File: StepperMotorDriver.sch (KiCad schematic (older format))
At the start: 15 parts, among them J2 Conn_01x04_Male, U1 DRV8825PWPR

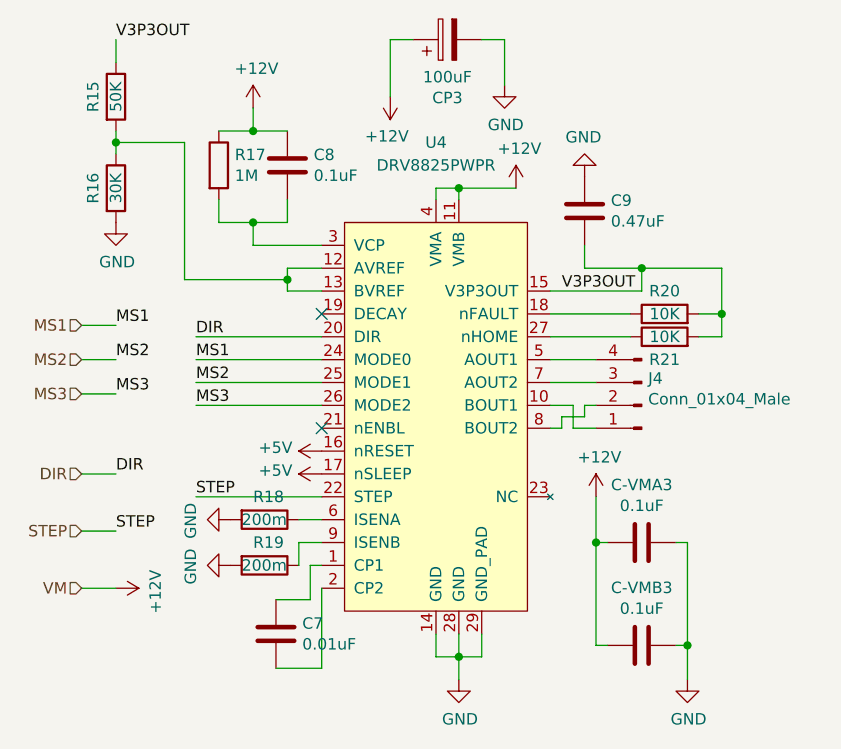
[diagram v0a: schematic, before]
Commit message: Test Pin
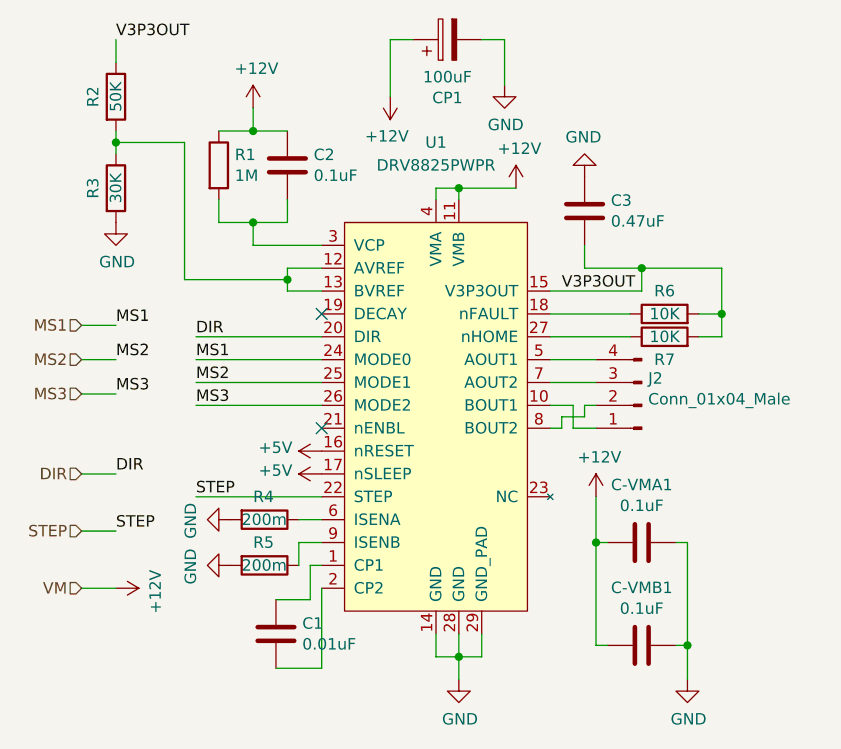
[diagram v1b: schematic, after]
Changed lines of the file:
@@
 $Descr A4 11693 8268
 encoding utf-8
-Sheet 3 10
+Sheet 4 10
 Title ""
 Date ""
@@
 AR Path="/5E601D92/5E5CA1CC" Ref="#PWR0118"  Part="1"
 AR Path="/5E6050A3/5E5CA1CC" Ref="#PWR0133"  Part="1"
-F 0 "#PWR0133" H 5950 4050 50  0001 C CNN
+F 0 "#PWR0101" H 5950 4050 50  0001 C CNN
 F 1 "GND" H 5955 4127 50  0000 C CNN
 F 2 "" H 5950 4300 50  0001 C CNN
@@
 AR Path="/5E601D92/5E5CAE8A" Ref="#PWR0119"  Part="1"
 AR Path="/5E6050A3/5E5CAE8A" Ref="#PWR0134"  Part="1"
-F 0 "#PWR0134" H 4450 2050 50  0001 C CNN
+F 0 "#PWR0102" H 4450 2050 50  0001 C CNN
 F 1 "GND" H 4455 2127 50  0000 C CNN
 F 2 "" H 4450 2300 50  0001 C CNN
@@
 AR Path="/5E601D92/5E5CB7B2" Ref="R10"  Part="1"
 AR Path="/5E6050A3/5E5CB7B2" Ref="R17"  Part="1"
-F 0 "R17" H 4970 2096 50  0000 L CNN
+F 0 "R1" H 4970 2096 50  0000 L CNN
 F 1 "1M" H 4970 2005 50  0000 L CNN
 F 2 "Resistor_SMD:R_0603_1608Metric_Pad1.05x0.95mm_HandSolder" V 4830 2050 50  0001 C CNN
@@
 AR Path="/5E601D92/5E5D2788" Ref="C6"  Part="1"
 AR Path="/5E6050A3/5E5D2788" Ref="C9"  Part="1"
-F 0 "C9" H 6615 2296 50  0000 L CNN
+F 0 "C3" H 6615 2296 50  0000 L CNN
 F 1 "0.47uF" H 6615 2205 50  0000 L CNN
 F 2 "Capacitor_SMD:C_0603_1608Metric_Pad1.05x0.95mm_HandSolder" H 6538 2100 50  0001 C CNN
@@
 AR Path="/5E601D92/5E5DA2EF" Ref="C5"  Part="1"
 AR Path="/5E6050A3/5E5DA2EF" Ref="C8"  Part="1"
-F 0 "C8" H 5315 2096 50  0000 L CNN
+F 0 "C2" H 5315 2096 50  0000 L CNN
 F 1 "0.1uF" H 5315 2005 50  0000 L CNN
 F 2 "Capacitor_SMD:C_0603_1608Metric_Pad1.05x0.95mm_HandSolder" H 5238 1900 50  0001 C CNN
@@
 AR Path="/5E601D92/5E5E742C" Ref="C4"  Part="1"
 AR Path="/5E6050A3/5E5E742C" Ref="C7"  Part="1"
-F 0 "C7" H 5265 4146 50  0000 L CNN
+F 0 "C1" H 5265 4146 50  0000 L CNN
 F 1 "0.01uF" H 5265 4055 50  0000 L CNN
 F 2 "Capacitor_SMD:C_0603_1608Metric_Pad1.05x0.95mm_HandSolder" H 5188 3950 50  0001 C CNN
@@
 AR Path="/5E601D92/5E5E8AA0" Ref="R11"  Part="1"
 AR Path="/5E6050A3/5E5E8AA0" Ref="R18"  Part="1"
-F 0 "R18" V 5000 3550 50  0000 L CNN
+F 0 "R4" V 5000 3550 50  0000 L CNN
 F 1 "200m" V 5100 3500 50  0000 L CNN
 F 2 "Resistor_SMD:R_0603_1608Metric_Pad1.05x0.95mm_HandSolder" V 5030 3600 50  0001 C CNN
@@
 AR Path="/5E601D92/5E5EA247" Ref="R12"  Part="1"
 AR Path="/5E6050A3/5E5EA247" Ref="R19"  Part="1"
-F 0 "R19" V 5000 3750 50  0000 L CNN
+F 0 "R5" V 5000 3750 50  0000 L CNN
 F 1 "200m" V 5100 3700 50  0000 L CNN
 F 2 "Resistor_SMD:R_0603_1608Metric_Pad1.05x0.95mm_HandSolder" V 5030 3800 50  0001 C CNN
@@
 AR Path="/5E601D92/5E5EAA71" Ref="#PWR0120"  Part="1"
 AR Path="/5E6050A3/5E5EAA71" Ref="#PWR0135"  Part="1"
-F 0 "#PWR0135" H 4950 3550 50  0001 C CNN
+F 0 "#PWR0105" H 4950 3550 50  0001 C CNN
 F 1 "GND" H 4955 3627 50  0000 C CNN
 F 2 "" H 4950 3800 50  0001 C CNN
@@
 AR Path="/5E601D92/5E5EB3DF" Ref="#PWR0121"  Part="1"
 AR Path="/5E6050A3/5E5EB3DF" Ref="#PWR0136"  Part="1"
-F 0 "#PWR0136" H 4950 3350 50  0001 C CNN
+F 0 "#PWR0106" H 4950 3350 50  0001 C CNN
 F 1 "GND" H 4955 3427 50  0000 C CNN
 F 2 "" H 4950 3600 50  0001 C CNN
@@
 AR Path="/5E601D92/5E5EC6B8" Ref="#PWR0122"  Part="1"
 AR Path="/5E6050A3/5E5EC6B8" Ref="#PWR0137"  Part="1"
-F 0 "#PWR0137" H 6500 1850 50  0001 C CNN
+F 0 "#PWR0107" H 6500 1850 50  0001 C CNN
 F 1 "GND" H 6505 1927 50  0000 C CNN
 F 2 "" H 6500 2100 50  0001 C CNN
@@
 AR Path="/5E601D92/5E5EE5E6" Ref="R13"  Part="1"
 AR Path="/5E6050A3/5E5EE5E6" Ref="R20"  Part="1"
-F 0 "R20" V 6950 2700 50  0000 C CNN
+F 0 "R6" V 6950 2700 50  0000 C CNN
 F 1 "10K" V 6850 2700 50  0000 C CNN
 F 2 "Resistor_SMD:R_0603_1608Metric_Pad1.05x0.95mm_HandSolder" V 6780 2700 50  0001 C CNN
@@
 AR Path="/5E601D92/5E5F31A6" Ref="R14"  Part="1"
 AR Path="/5E6050A3/5E5F31A6" Ref="R21"  Part="1"
-F 0 "R21" V 6750 2800 50  0000 C CNN
+F 0 "R7" V 6750 2800 50  0000 C CNN
 F 1 "10K" V 6850 2800 50  0000 C CNN
 F 2 "Resistor_SMD:R_0603_1608Metric_Pad1.05x0.95mm_HandSolder" V 6780 2800 50  0001 C CNN
@@
 AR Path="/5E601D92/5E5FA975" Ref="R8"  Part="1"
 AR Path="/5E6050A3/5E5FA975" Ref="R15"  Part="1"
-F 0 "R15" V 4350 1750 50  0000 C CNN
+F 0 "R2" V 4350 1750 50  0000 C CNN
 F 1 "50K" V 4450 1750 50  0000 C CNN
 F 2 "Resistor_SMD:R_0603_1608Metric_Pad1.05x0.95mm_HandSolder" V 4380 1750 50  0001 C CNN
@@
 AR Path="/5E601D92/5E5FD16F" Ref="R9"  Part="1"
 AR Path="/5E6050A3/5E5FD16F" Ref="R16"  Part="1"
-F 0 "R16" V 4350 2150 50  0000 C CNN
+F 0 "R3" V 4350 2150 50  0000 C CNN
 F 1 "30K" V 4450 2150 50  0000 C CNN
 F 2 "Resistor_SMD:R_0603_1608Metric_Pad1.05x0.95mm_HandSolder" V 4380 2150 50  0001 C CNN
@@
 AR Path="/5E601D92/5E60B6B4" Ref="J3"  Part="1"
 AR Path="/5E6050A3/5E60B6B4" Ref="J4"  Part="1"
-F 0 "J4" H 6722 2982 50  0000 R CNN
+F 0 "J2" H 6722 2982 50  0000 R CNN
 F 1 "Conn_01x04_Male" H 6722 3073 50  0000 R CNN
 F 2 "Connector_Molex:Molex_PicoBlade_53047-0410_1x04_P1.25mm_Vertical" H 6750 3100 50  0001 C CNN
@@
 AR Path="/5E601D92/5E6128D6" Ref="C-VMA2"  Part="1"
 AR Path="/5E6050A3/5E6128D6" Ref="C-VMA3"  Part="1"
-F 0 "C-VMA3" V 6498 3700 50  0000 C CNN
+F 0 "C-VMA1" V 6498 3700 50  0000 C CNN
 F 1 "0.1uF" V 6589 3700 50  0000 C CNN
 F 2 "Capacitor_SMD:C_0603_1608Metric_Pad1.05x0.95mm_HandSolder" H 6788 3550 50  0001 C CNN
@@
 AR Path="/5E601D92/5E61EB61" Ref="#PWR0123"  Part="1"
 AR Path="/5E6050A3/5E61EB61" Ref="#PWR0138"  Part="1"
-F 0 "#PWR0138" H 6550 3350 50  0001 C CNN
+F 0 "#PWR0109" H 6550 3350 50  0001 C CNN
 F 1 "+12V" H 6565 3673 50  0000 C CNN
 F 2 "" H 6550 3500 50  0001 C CNN
@@
 AR Path="/5E601D92/5E61FED4" Ref="#PWR0124"  Part="1"
 AR Path="/5E6050A3/5E61FED4" Ref="#PWR0139"  Part="1"
-F 0 "#PWR0139" H 6950 4050 50  0001 C CNN
+F 0 "#PWR0110" H 6950 4050 50  0001 C CNN
 F 1 "GND" H 6955 4127 50  0000 C CNN
 F 2 "" H 6950 4300 50  0001 C CNN
@@
 AR Path="/5E601D92/5E61E3FE" Ref="C-VMB2"  Part="1"
 AR Path="/5E6050A3/5E61E3FE" Ref="C-VMB3"  Part="1"
-F 0 "C-VMB3" V 6498 4150 50  0000 C CNN
+F 0 "C-VMB1" V 6498 4150 50  0000 C CNN
 F 1 "0.1uF" V 6589 4150 50  0000 C CNN
 F 2 "Capacitor_SMD:C_0603_1608Metric_Pad1.05x0.95mm_HandSolder" H 6788 4000 50  0001 C CNN
@@
 AR Path="/5E601D92/5E6259D9" Ref="#PWR0125"  Part="1"
 AR Path="/5E6050A3/5E6259D9" Ref="#PWR0140"  Part="1"
-F 0 "#PWR0140" H 5350 3250 50  0001 C CNN
+F 0 "#PWR0111" H 5350 3250 50  0001 C CNN
 F 1 "+5V" V 5365 3528 50  0000 L CNN
 F 2 "" H 5350 3400 50  0001 C CNN
@@
 AR Path="/5E601D92/5E627A58" Ref="#PWR0126"  Part="1"
 AR Path="/5E6050A3/5E627A58" Ref="#PWR0141"  Part="1"
-F 0 "#PWR0141" H 5350 3150 50  0001 C CNN
+F 0 "#PWR0112" H 5350 3150 50  0001 C CNN
 F 1 "+5V" V 5365 3428 50  0000 L CNN
 F 2 "" H 5350 3300 50  0001 C CNN
@@
 AR Path="/5E601D92/5E644E90" Ref="#PWR0128"  Part="1"
 AR Path="/5E6050A3/5E644E90" Ref="#PWR0143"  Part="1"
-F 0 "#PWR0143" H 6150 1450 50  0001 C CNN
+F 0 "#PWR0114" H 6150 1450 50  0001 C CNN
 F 1 "GND" H 6155 1527 50  0000 C CNN
 F 2 "" H 6150 1700 50  0001 C CNN
@@
 AR Path="/5E601D92/5E647686" Ref="#PWR0129"  Part="1"
 AR Path="/5E6050A3/5E647686" Ref="#PWR0144"  Part="1"
-F 0 "#PWR0144" H 5650 1600 50  0001 C CNN
+F 0 "#PWR0115" H 5650 1600 50  0001 C CNN
 F 1 "+12V" H 5665 1923 50  0000 C CNN
 F 2 "" H 5650 1750 50  0001 C CNN
@@
 AR Path="/5E601D92/5E5BDB2A" Ref="U3"  Part="1"
 AR Path="/5E6050A3/5E5BDB2A" Ref="U4"  Part="1"
-F 0 "U4" H 5850 3850 50  0000 C CNN
+F 0 "U1" H 5850 3850 50  0000 C CNN
 F 1 "DRV8825PWPR" H 5850 3750 50  0000 C CNN
 F 2 "Package_SO:HTSSOP-28-1EP_4.4x9.7mm_P0.65mm_EP3.4x9.5mm_ThermalVias" H 5750 2900 50  0001 L BNN
@@
 AR Path="/5E601D92/5E636B79" Ref="#PWR0130"  Part="1"
 AR Path="/5E6050A3/5E636B79" Ref="#PWR0145"  Part="1"
-F 0 "#PWR0145" H 6200 2000 50  0001 C CNN
+F 0 "#PWR0103" H 6200 2000 50  0001 C CNN
 F 1 "+12V" H 6215 2323 50  0000 C CNN
 F 2 "" H 6200 2150 50  0001 C CNN
@@
 AR Path="/5E601D92/5E64ABEC" Ref="CP2"  Part="1"
 AR Path="/5E6050A3/5E64ABEC" Ref="CP3"  Part="1"
-F 0 "CP3" V 5645 1500 50  0000 C CNN
+F 0 "CP1" V 5645 1500 50  0000 C CNN
 F 1 "100uF" V 5736 1500 50  0000 C CNN
 F 2 "Capacitor_Tantalum_SMD:CP_EIA-3528-21_Kemet-B_Pad1.50x2.35mm_HandSolder" H 5938 1350 50  0001 C CNN
@@
 AR Path="/5E601D92/5E68EF50" Ref="#PWR0131"  Part="1"
 AR Path="/5E6050A3/5E68EF50" Ref="#PWR0146"  Part="1"
-F 0 "#PWR0146" H 5050 1650 50  0001 C CNN
+F 0 "#PWR0104" H 5050 1650 50  0001 C CNN
 F 1 "+12V" H 5065 1973 50  0000 C CNN
 F 2 "" H 5050 1800 50  0001 C CNN
@@
 AR Path="/5E601D92/5E5FEB06" Ref="#PWR0132"  Part="1"
 AR Path="/5E6050A3/5E5FEB06" Ref="#PWR0147"  Part="1"
-F 0 "#PWR0147" H 4450 3750 50  0001 C CNN
+F 0 "#PWR0148" H 4450 3750 50  0001 C CNN
 F 1 "+12V" H 4465 4073 50  0000 C CNN
 F 2 "" H 4450 3900 50  0001 C CNN
